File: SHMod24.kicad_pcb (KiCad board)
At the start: 2 copper layers, 49.5 x 49.5 mm, 65 parts, among them IC1 ArduinoProMini, J1 Conn_02x14_Odd_Even, J2 Conn_01x01, J3 Conn_01x01, J4 RESET, J5 12V, J6 GND, J9 Screw_Terminal_01x02, Q1 FS8205A, Q2 AO3400A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

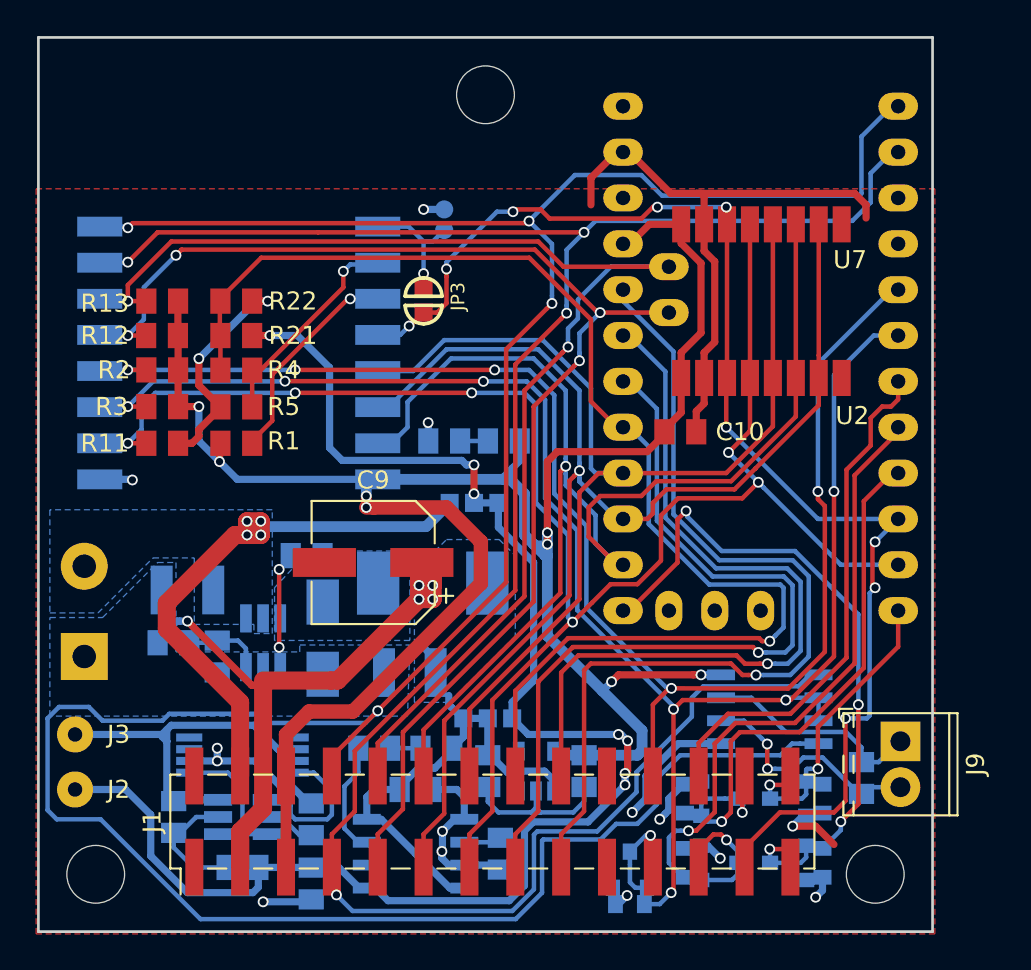
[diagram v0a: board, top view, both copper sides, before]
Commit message: fix LDO no GND && minor trace improvements
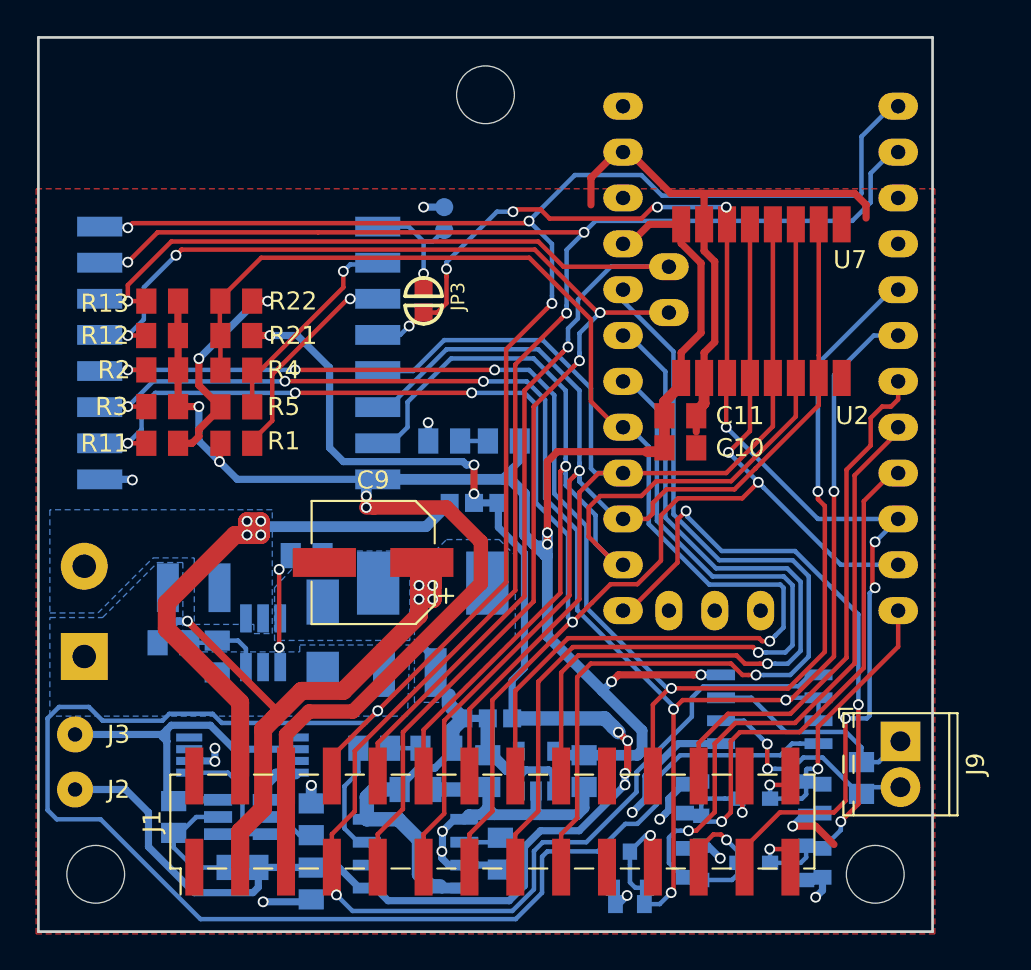
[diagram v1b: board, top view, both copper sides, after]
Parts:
- added C11: 100n, Capacitor_SMD:C_0805_2012Metric, F.Cu at (86.4, 83.2)
- R6: value 1k2 -> 2k2
- moved C10 0.89 mm to (86.4, 85.0)
- moved C7 0.37 mm to (59.4, 92.7)
- moved J6 0.13 mm to (73.3, 71.6)
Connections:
- C1 pad 2: Net-(C1-Pad2) -> GND
- C2 pad 2: Net-(C1-Pad2) -> GND
- U3 pad 2: Net-(C1-Pad2) -> GND
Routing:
- net Net-(C1-Pad2): track 9.10 -> 0.00 mm
- net GND: track 92.5 -> 99.2 mm, vias 16 -> 17
- net Net-(Q1-Pad4): track 8.21 -> 2.73 mm
- net +5V: track 64.7 -> 66.5 mm
- net RX: track 125.8 -> 125.3 mm
- net TX: track 162.0 -> 161.4 mm
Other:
- net class 08 added: clearance 0.2, trace_width 0.8, via_dia 0.8, via_drill 0.6

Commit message: more layout improvements
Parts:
- added JP4: ESP_MOSFET, LeoDJ-kicad:SOLDER-JUMPER_1-WAY, F.Cu at (92.6, 84.8)
- added JP5: ESP_MOSFET, LeoDJ-kicad:SOLDER-JUMPER_1-WAY, F.Cu at (92.6, 86.2)
- JP3: moved to B.Cu
- moved C6 0.76 mm to (66.4, 90.9)
- moved C7 0.76 mm to (60.2, 92.7)
- moved C8 0.76 mm to (72.1, 97.4)
- moved C9 0.76 mm to (69.3, 90.6)
- moved D1 0.76 mm to (67.3, 95.5)
- moved L1 0.76 mm to (73.4, 92.5)
- moved R10 0.76 mm to (61.5, 96.5)
- moved R9 0.76 mm to (59.0, 95.8)
- moved U6 0.76 mm to (64.0, 95.8)
- moved J3 0.51 mm to (52.8, 101.3)
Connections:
- IC1 pad 29: GND -> Net-(IC1-Pad29)
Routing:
- net P06: track 33.5 -> 40.7 mm, vias 2 -> 4
- net P05: track 41.6 -> 48.3 mm, vias 2 -> 4
- net GPIO13: track 74.6 -> 77.7 mm, vias 1 -> 3
- net GPIO12: track 71.8 -> 74.1 mm
- net P10: track 39.5 -> 41.5 mm, vias 4 -> 5
- net TX: track 161.4 -> 159.5 mm
- net VCC: track 32.2 -> 30.4 mm
- net +3V3: track 125.1 -> 123.7 mm
- net P09: track 20.8 -> 21.8 mm, vias 2 -> 3
- net Net-(C6-Pad1): track 6.47 -> 7.36 mm
- net GPIO2: track 99.4 -> 100.2 mm, vias 8 -> 9
- net RX: track 125.3 -> 124.7 mm
- net GND: track 99.2 -> 99.0 mm, vias 17 -> 23
- net GPIO16: track 74.0 -> 73.9 mm, vias 9 -> 7
- net Net-(J4-Pad1): vias 1 -> 0

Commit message: more improvements
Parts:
- added R24: 10k, Resistor_SMD:R_0805_2012Metric, F.Cu at (59.7, 74.7)
- J9: moved to B.Cu
- moved J9 2.67 mm to (98.7, 98.6)
- moved J2 0.51 mm to (53.3, 103.9)
- moved J3 0.51 mm to (53.3, 101.3)
- moved D1 0.13 mm to (67.4, 95.5)
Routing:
- net Net-(J4-Pad1): track 7.62 -> 16.8 mm, vias 0 -> 1
- net +3V3: track 123.7 -> 126.0 mm
- net Net-(J9-Pad2): track 14.0 -> 15.8 mm
- net Net-(J9-Pad1): track 12.6 -> 14.5 mm
- net CS: track 95.8 -> 97.3 mm
- net SDA: track 72.1 -> 71.1 mm
- net SCL: track 71.3 -> 72.0 mm
- net TX: track 159.5 -> 158.9 mm
- net A0: track 73.4 -> 74.1 mm
- net -BATT: track 19.3 -> 18.8 mm
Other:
- board text added: "+"
- board text added: "-"
- board text added: "GND GND 5V VCC 3V3 3V3 RX TX SDA SCL MISO MOSI CS SCK A1 A0 A3 A2 GND GND P03 P02 P05 P04 P07 P06 P10 P09"
- board text added: "LiPo"
- board text added: "Reset"
- board text added: "SHMod24 v1.0"
- board text added: "https://github.com/ LeoDJ/SHMod24"

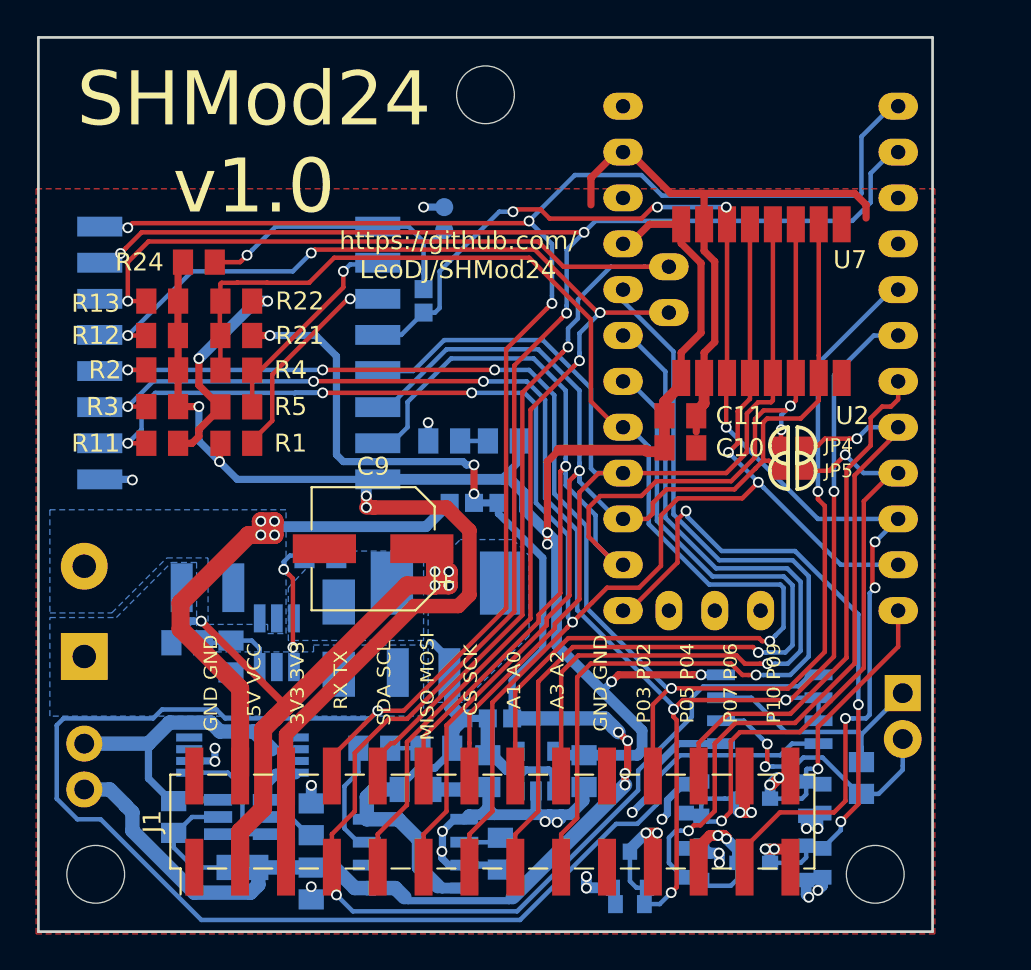
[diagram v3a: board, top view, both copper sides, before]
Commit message: improve routing for 485 transceiver
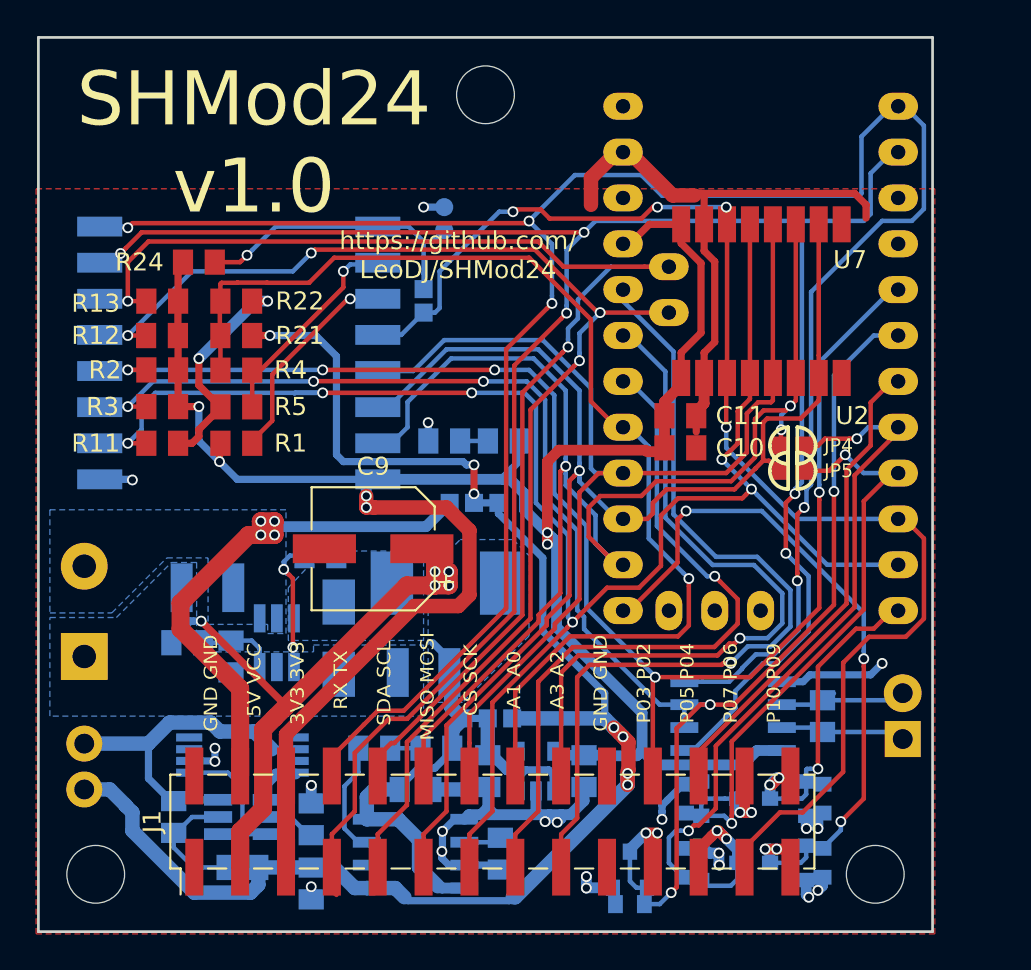
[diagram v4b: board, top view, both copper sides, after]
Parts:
- moved R15 4.05 mm to (94.2, 99.8), turned to 90 degrees
- moved J9 2.54 mm to (98.7, 101.1), turned to 90 degrees
- moved U8 2.07 mm to (89.3, 99.8), turned to 0 degrees
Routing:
- net TX: track 158.9 -> 127.7 mm, vias 4 -> 5
- net A0: track 74.1 -> 64.1 mm
- net Net-(J9-Pad2): track 15.8 -> 7.32 mm, vias 2 -> 0
- net A1: track 47.0 -> 39.7 mm
- net Net-(J9-Pad1): track 14.5 -> 8.05 mm
- net A3: track 51.7 -> 47.7 mm
- net A2: track 43.9 -> 40.2 mm
- net P04: track 29.1 -> 26.6 mm
- net GPIO0: track 82.1 -> 79.9 mm
- net GPIO2: track 100.2 -> 98.0 mm, vias 9 -> 8
- net P05: track 48.3 -> 46.5 mm
- net +3V3: track 126.0 -> 127.5 mm, vias 8 -> 6
- net P06: track 40.7 -> 39.2 mm
- net GPIO16: track 73.9 -> 75.3 mm, vias 7 -> 4
- net GND: track 99.0 -> 97.8 mm
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
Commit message: final improvements: better track layout, silk screen symbols
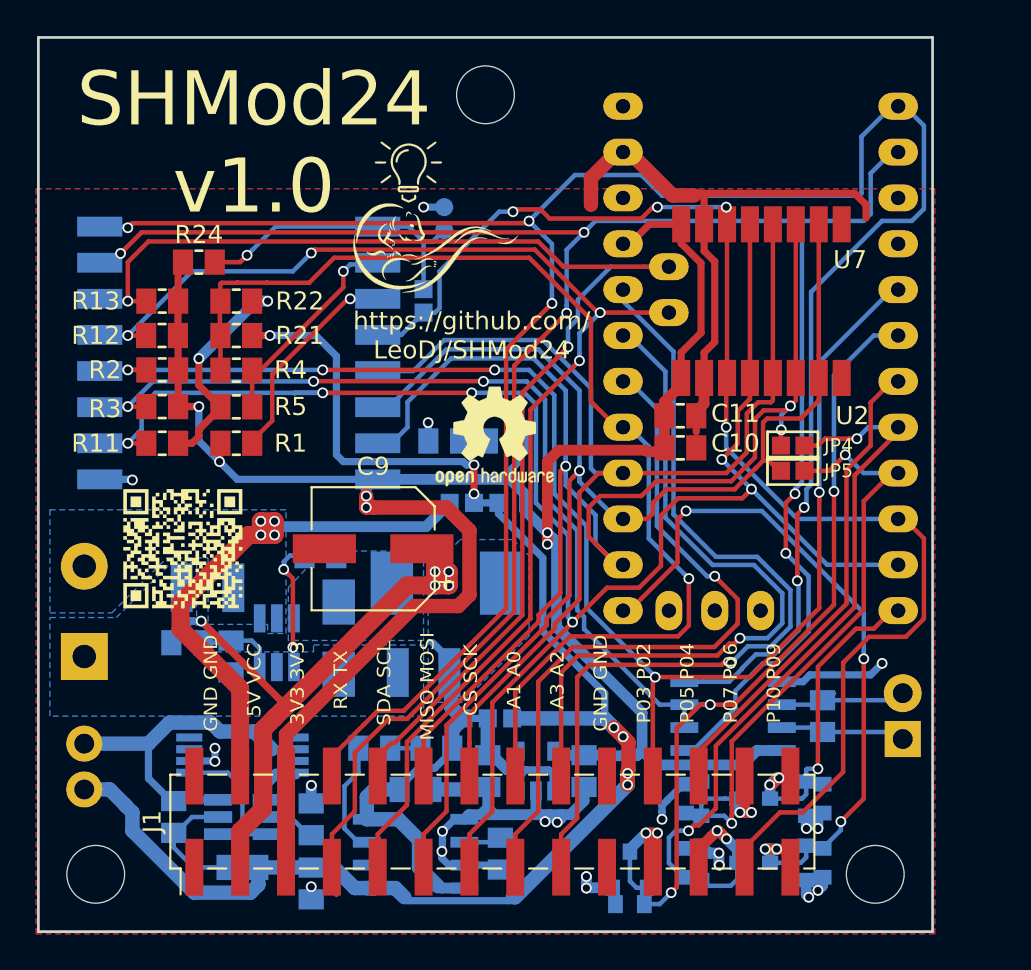
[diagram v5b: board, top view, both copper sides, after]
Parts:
- added LOGO1: Logo_Open_Hardware_Small, Symbol:OSHW-Logo2_7.3x6mm_SilkScreen, F.Cu at (76.1, 84.3)
- added SYM1: SYM_Arrow_Tiny, leodj-kicad:Otter_Lightbulb_smaller, F.Cu at (72.8, 72.0)
- added SYM2: SYM_Arrow_Tiny, leodj-kicad:QR_Code_SHMod24, F.Cu at (58.8, 90.6)
- C1, C10, C11, C2, C3, C4, C5, C6: footprint Capacitor_SMD:C_0805_2012Metric -> LeoDJ-kicad:C_0805_2012Metric
- R1, R10, R11, R12, R13, R14, R15, R2, R21, R22, R23, R24, R3, R4, R5, R6, R7, R8, R9: footprint Resistor_SMD:R_0805_2012Metric -> LeoDJ-kicad:R_0805_2012Metric

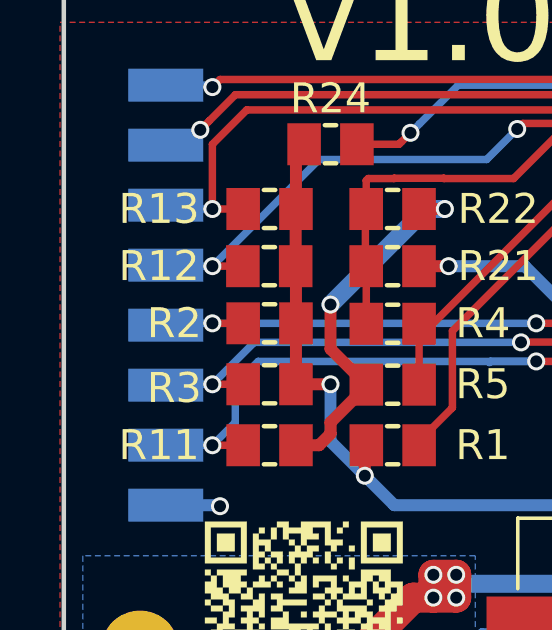
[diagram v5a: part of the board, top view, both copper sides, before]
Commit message: add RS485 connector markings
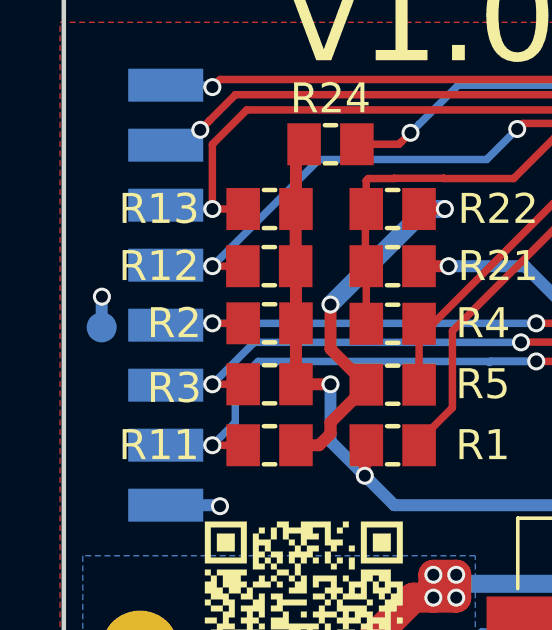
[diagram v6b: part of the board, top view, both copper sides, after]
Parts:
- added J8: GND, TestPoint:TestPoint_Pad_D1.0mm, B.Cu at (52.1, 80.8)
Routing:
- net GND: track 97.8 -> 98.8 mm, vias 23 -> 24
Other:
- board text added: "A"
- board text added: "B"
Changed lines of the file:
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@@
   (general
     (thickness 1.6)
-    (drawings 13)
-    (tracks 1109)
+    (drawings 15)
+    (tracks 1112)
     (zones 0)
-    (modules 72)
+    (modules 73)
     (nets 59)
   )
@@
     (46 B.CrtYd user hide)
     (47 F.CrtYd user hide)
-    (48 B.Fab user)
-    (49 F.Fab user)
+    (48 B.Fab user hide)
+    (49 F.Fab user hide)
   )
   (setup
@@
     (add_net VCC)
   )
+  (module TestPoint:TestPoint_Pad_D1.0mm (layer B.Cu)
+    (at 52.062809 80.7795)
+    (descr "SMD pad as test Point, diameter 1.0mm")
+    (tags "test point SMD pad")
+    (attr virtual)
+    (fp_text reference J8 (at 0.007191 1.6435 90) (layer B.SilkS)
+      (effects (font (size 1 1) (thickness 0.15)) (justify mirror))
+    )
+    (fp_text value GND (at 0 -1.55) (layer B.Fab)
+      (effects (font (size 1 1) (thickness 0.15)) (justify mirror))
+    )
+    (fp_text user %R (at 0 1.45) (layer B.Fab)
+      (effects (font (size 1 1) (thickness 0.15)) (justify mirror))
+    )
+    (fp_circle (center 0 0) (end 1 0) (layer B.CrtYd) (width 0.05))
+    (fp_circle (center 0 0) (end 0 -0.7) (layer B.SilkS) (width 0.12))
+    (pad 1 smd circle (at 0 0) (size 1 1) (layers B.Cu B.Mask)
+      (net 6 GND))
+  )
   (module LeoDJ-kicad:SOLDER-JUMPER_2-WAY (layer B.Cu)
     (at 74.93 88.011 180)
@@
     (tags capacitor)
     (attr smd)
-    (fp_text reference C2 (at 0 -1.651 270) (layer B.SilkS)
+    (fp_text reference C2 (at 2.413 0) (layer B.SilkS)
       (effects (font (size 1 1) (thickness 0.15)) (justify mirror))
     )
@@
     (tags SOT-23-5)
     (attr smd)
-    (fp_text reference U3 (at -2.413 1.016 180) (layer B.SilkS)
+    (fp_text reference U3 (at -2.413 0.381 180) (layer B.SilkS)
       (effects (font (size 1 1) (thickness 0.15)) (justify mirror))
     )
@@
     (descr "IC, ARDUINO_PRO_MINI x 0,6\"")
     (tags "DIL ARDUINO PRO MINI")
-    (fp_text reference IC1 (at 16.129 -7.239) (layer B.SilkS)
+    (fp_text reference IC1 (at 16.129 8.255) (layer B.SilkS)
       (effects (font (size 0.8 0.8) (thickness 0.16)) (justify mirror))
     )
@@
     )
     (model ${MYSLOCAL}/mysensors.3dshapes/mysensors_arduino.3dshapes/arduino_pro_mini.wrl
-      (offset (xyz -1.269999980926514 0 12.19199981689453))
+      (offset (xyz -1.27 0 0.75))
       (scale (xyz 0.395 0.395 0.395))
       (rotate (xyz 0 0 180))
@@
     )
     (model ${MYSLOCAL}/mysensors.3dshapes/w.lain.3dshapes/smd_leds/led_0603.wrl
-      (offset (xyz -7.619999885559082 0 13.01749980449676))
+      (offset (xyz -7.62 0 1.56))
       (scale (xyz 1 1 1))
       (rotate (xyz 0 0 0))
     )
     (model ${MYSLOCAL}/mysensors.3dshapes/w.lain.3dshapes/smd_leds/led_0603.wrl
-      (offset (xyz 13.96999979019165 -4.444999933242798 13.01749980449676))
+      (offset (xyz 13.97 -4.445 1.56))
       (scale (xyz 1 1 1))
       (rotate (xyz 0 0 0))
@@
     )
   )
+  (gr_text B (at 99.187 103.505) (layer B.SilkS)
+    (effects (font (size 1 1) (thickness 0.15)) (justify mirror))
+  )
+  (gr_text A (at 99.187 96.266) (layer B.SilkS)
+    (effects (font (size 1 1) (thickness 0.15)) (justify mirror))
+  )
   (gr_text " GND GND \n\n  5V VCC \n\n 3V3 3V3 \n\n  RX TX  \n\n SDA SCL \n\nMISO MOSI\n\n  CS SCK \n\n  A1 A0  \n\n  A3 A2  \n\n GND GND \n\n P03 P02 \n\n P05 P04 \n\n P07 P06 \n\n P10 P09 \n" (at 75.946 98.171 90) (layer F.SilkS)
     (effects (font (size 0.745 0.8) (thickness 0.15)))
@@
     (effects (font (size 3 3) (thickness 0.5)))
   )
-  (gr_text + (at 51.435 88.138) (layer B.SilkS)
+  (gr_text + (at 52.07 88.138) (layer B.SilkS)
     (effects (font (size 1 1) (thickness 0.15)) (justify mirror))
   )
-  (gr_text - (at 51.435 99.695) (layer B.SilkS)
+  (gr_text - (at 52.07 99.822) (layer B.SilkS)
     (effects (font (size 1 1) (thickness 0.15)) (justify mirror))
   )
@@
   (segment (start 83.185 68.58) (end 83.53425 68.58) (width 0.8) (layer F.Cu) (net 6))
   (segment (start 83.53425 68.58) (end 85.935249 70.980999) (width 0.8) (layer F.Cu) (net 6))
+  (via (at 52.07 79.756) (size 0.6) (drill 0.4) (layers F.Cu B.Cu) (net 6))
+  (segment (start 52.062809 80.7795) (end 52.062809 79.763191) (width 0.4) (layer B.Cu) (net 6))
+  (segment (start 52.062809 79.763191) (end 52.07 79.756) (width 0.4) (layer B.Cu) (net 6))
   (segment (start 95.295 81.09) (end 95.295 80.6) (width 0.25) (layer F.Cu) (net 7))
   (via (at 81.915 77.47) (size 0.6) (drill 0.4) (layers F.Cu B.Cu) (net 13))
